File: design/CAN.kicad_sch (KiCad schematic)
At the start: 4 parts, among them U401 SN65HVD232

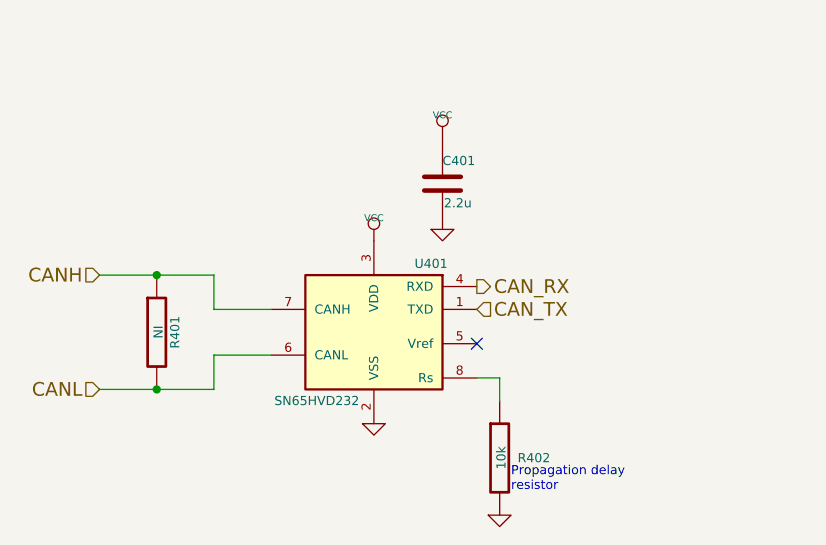
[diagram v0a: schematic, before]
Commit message: Actualización VESC6.4
Actualización a esquemáticos de VESC6.4, faltan asignación de huellas y descripción a cada elemento.
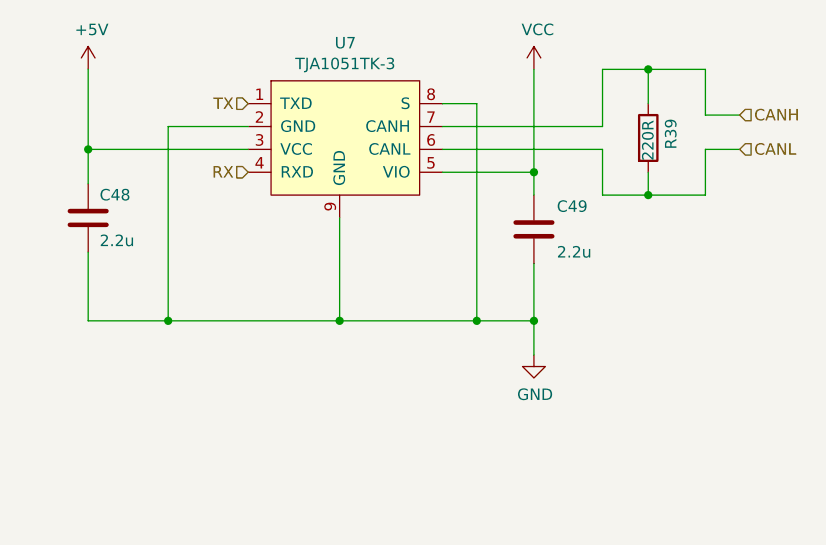
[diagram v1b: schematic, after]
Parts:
- removed C401: 2.2u, CRF1:SMD-0603_c, symbol BLDC_4-rescue1:C-RESCUE-BLDC_4
- removed R401: NI, CRF1:SMD-0603_r, symbol BLDC_4-rescue1:R-RESCUE-BLDC_4
- removed R402: 10k, CRF1:SMD-0603_r, symbol BLDC_4-rescue1:R-RESCUE-BLDC_4
- removed U401: SN65HVD232, CRF1:SOIC-8-W, symbol BLDC_4-rescue1:MCP2551-I/SN-RESCUE-BLDC_4
- added C48, C49: 2.2u, symbol Device:C
- added R39: 220R, symbol Device:R
- added U7: TJA1051TK-3, Package_DFN_QFN:DFN-8-1EP_3x3mm_P0.65mm_EP1.55x2.4mm, symbol bldc:TJA1051TK-3
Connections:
- net CANH: now also R39.1, U7.7 (CANH)
- net CANL: now also R39.2, U7.6 (CANL)
- net GND: now also C48.2, C49.2, U7.2 (GND), U7.8 (S), U7.9 (GND)
- net VCC: now also C49.1, U7.5 (VIO)
- new net +5V: C48.1, U7.3 (VCC)
- new net RX: U7.4 (RXD)
- new net TX: U7.1 (TXD)
- no-connect marks 1 -> 0
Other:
- note removed: "Propagation delay resistor"
- company: Benjamin Vedder -> UTN
- title: BLDC Driver 4.11 -> bldc-controller-edp
